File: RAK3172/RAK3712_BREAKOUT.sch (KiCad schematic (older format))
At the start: 3 parts, among them J1 Conn_01x20_Male, J2 Conn_01x20_Male, U1 RAK11300

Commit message: started RAK3172 symbol
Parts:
- removed U1: RAK11300, RAKWIRELESS:RAK11300, symbol RAKWIRELESS:RAK11300
- added U?: RAK3712, RAKWIRELESS:RAK3712, symbol RAKWIRELESS:RAK3712
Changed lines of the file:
@@
 $EndDescr
-$Comp
-L RAKWIRELESS:RAK11300 U1
-U 1 1 61FAC138
-P 5700 3250
-F 0 "U1" H 5700 2061 50  0000 C CNN
-F 1 "RAK11300" H 5700 1970 50  0000 C CNN
-F 2 "RAKWIRELESS:RAK11300" H 5900 3550 50  0001 C CNN
-F 3 "https://site-file.fomillesite.com/1260815565112336386/1427562149389201410.pdf" H 5900 3550 50  0001 C CNN
-	1    5700 3250
-	1    0    0    -1
-$EndComp
 $Comp
 L Connector:Conn_01x20_Male J1
@@
 Wire Wire Line
 	5900 2150 5900 1950
+$Comp
+L RAKWIRELESS:RAK3712 U?
+U 1 1 621E74F6
+P 4100 5900
+F 0 "U?" H 4100 4711 50  0000 C CNN
+F 1 "RAK3712" H 4100 4620 50  0000 C CNN
+F 2 "RAKWIRELESS:RAK3712" H 4300 6200 50  0001 C CNN
+F 3 "https://site-file.fomillesite.com/1260815565112336386/1427562149389201410.pdf" H 4300 6200 50  0001 C CNN
+	1    4100 5900
+	1    0    0    -1
+$EndComp
 $EndSCHEMATC

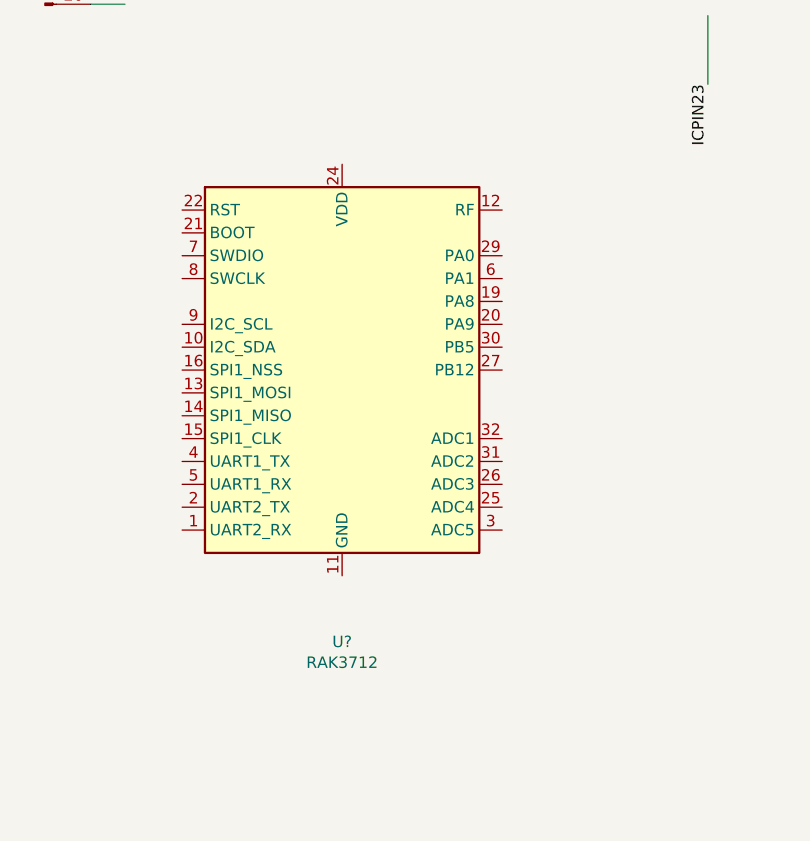
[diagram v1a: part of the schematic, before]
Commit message: sch:(DIL_BREAKOUT_PCB RAK 3712)changing pins
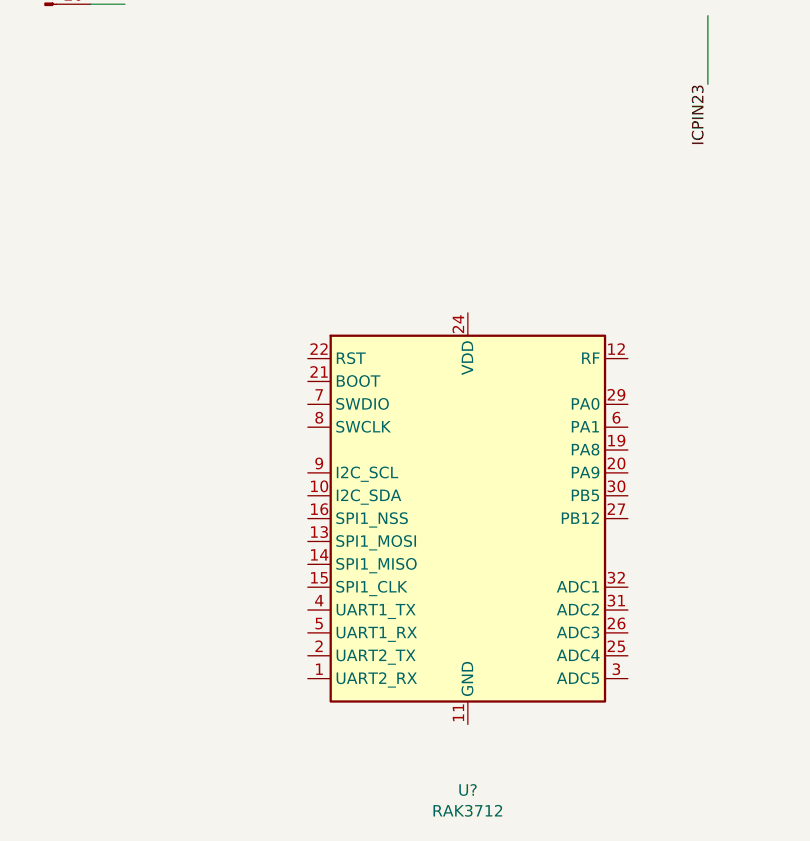
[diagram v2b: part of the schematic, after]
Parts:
- removed U?: RAK3712, RAKWIRELESS:RAK3712, symbol RAKWIRELESS:RAK3712
- added U?: RAK3712, RAKWIRELESS:RAK3712, symbol RAKWIRELESS:RAK3712
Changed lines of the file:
@@
 $Comp
 L RAKWIRELESS:RAK3712 U?
-U 1 1 621E74F6
-P 4100 5900
-F 0 "U?" H 4100 4711 50  0000 C CNN
-F 1 "RAK3712" H 4100 4620 50  0000 C CNN
-F 2 "RAKWIRELESS:RAK3712" H 4300 6200 50  0001 C CNN
-F 3 "https://site-file.fomillesite.com/1260815565112336386/1427562149389201410.pdf" H 4300 6200 50  0001 C CNN
-	1    4100 5900
+U 1 1 621FE862
+P 4650 6550
+F 0 "U?" H 4650 5361 50  0000 C CNN
+F 1 "RAK3712" H 4650 5270 50  0000 C CNN
+F 2 "RAKWIRELESS:RAK3712" H 4850 6850 50  0001 C CNN
+F 3 "https://site-file.fomillesite.com/1260815565112336386/1427562149389201410.pdf" H 4850 6850 50  0001 C CNN
+	1    4650 6550
 	1    0    0    -1
 $EndComp

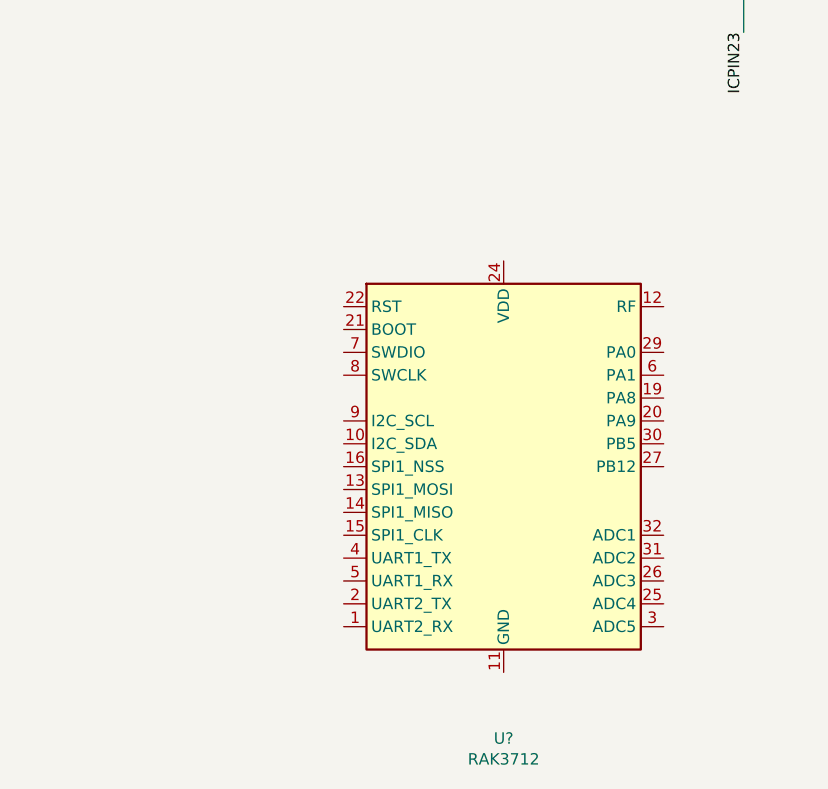
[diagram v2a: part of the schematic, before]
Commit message: sch:(DIL_BREAKOUT_PCB RAK 3712)pins arranged
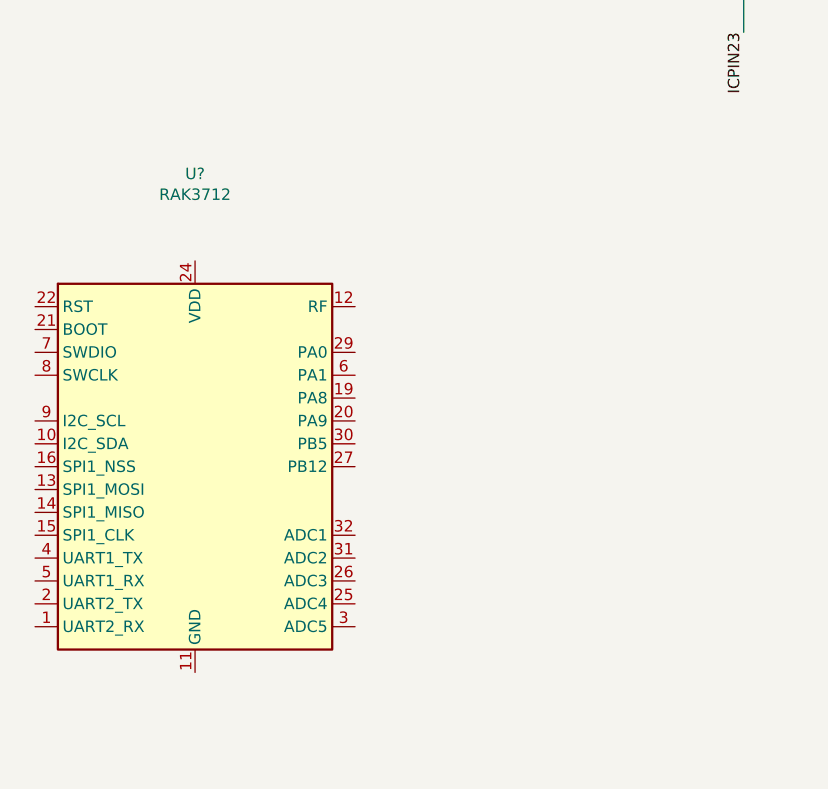
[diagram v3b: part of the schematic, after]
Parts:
- removed U?: RAK3712, RAKWIRELESS:RAK3712, symbol RAKWIRELESS:RAK3712
- added U?: RAK3712, RAKWIRELESS:RAK3712, symbol RAKWIRELESS:RAK3712
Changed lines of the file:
@@
 $Comp
 L RAKWIRELESS:RAK3712 U?
-U 1 1 621FE862
-P 4650 6550
-F 0 "U?" H 4650 5361 50  0000 C CNN
-F 1 "RAK3712" H 4650 5270 50  0000 C CNN
-F 2 "RAKWIRELESS:RAK3712" H 4850 6850 50  0001 C CNN
-F 3 "https://site-file.fomillesite.com/1260815565112336386/1427562149389201410.pdf" H 4850 6850 50  0001 C CNN
-	1    4650 6550
+U 1 1 621F85E6
+P 3300 6550
+F 0 "U?" H 3300 7831 50  0000 C CNN
+F 1 "RAK3712" H 3300 7740 50  0000 C CNN
+F 2 "RAKWIRELESS:RAK3712" H 3500 6850 50  0001 C CNN
+F 3 "https://site-file.fomillesite.com/1260815565112336386/1427562149389201410.pdf" H 3500 6850 50  0001 C CNN
+	1    3300 6550
 	1    0    0    -1
 $EndComp

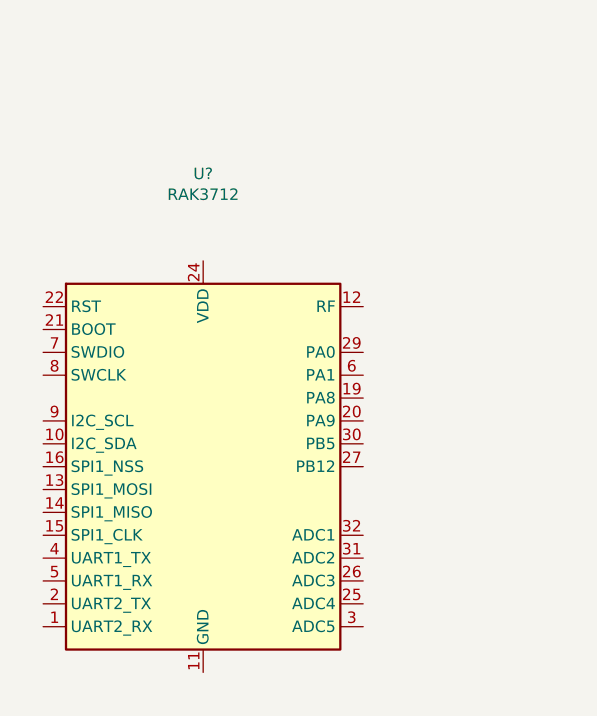
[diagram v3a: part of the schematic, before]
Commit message: sch:(DIL_BREAKOUT_PCB RAK 3712)shrinked
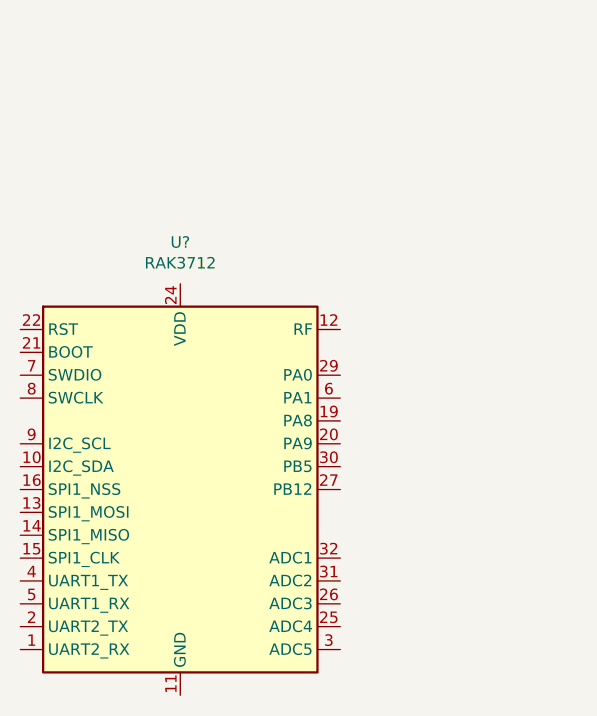
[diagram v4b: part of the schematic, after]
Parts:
- removed U?: RAK3712, RAKWIRELESS:RAK3712, symbol RAKWIRELESS:RAK3712
- added U?: RAK3712, RAKWIRELESS:RAK3712, symbol RAKWIRELESS:RAK3712
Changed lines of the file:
@@
 $Comp
 L RAKWIRELESS:RAK3712 U?
-U 1 1 621F85E6
-P 3300 6550
-F 0 "U?" H 3300 7831 50  0000 C CNN
-F 1 "RAK3712" H 3300 7740 50  0000 C CNN
-F 2 "RAKWIRELESS:RAK3712" H 3500 6850 50  0001 C CNN
-F 3 "https://site-file.fomillesite.com/1260815565112336386/1427562149389201410.pdf" H 3500 6850 50  0001 C CNN
-	1    3300 6550
+U 1 1 621FE0F5
+P 3200 6650
+F 0 "U?" H 3200 7731 50  0000 C CNN
+F 1 "RAK3712" H 3200 7640 50  0000 C CNN
+F 2 "RAKWIRELESS:RAK3712" H 3400 6950 50  0001 C CNN
+F 3 "https://site-file.fomillesite.com/1260815565112336386/1427562149389201410.pdf" H 3400 6950 50  0001 C CNN
+	1    3200 6650
 	1    0    0    -1
 $EndComp

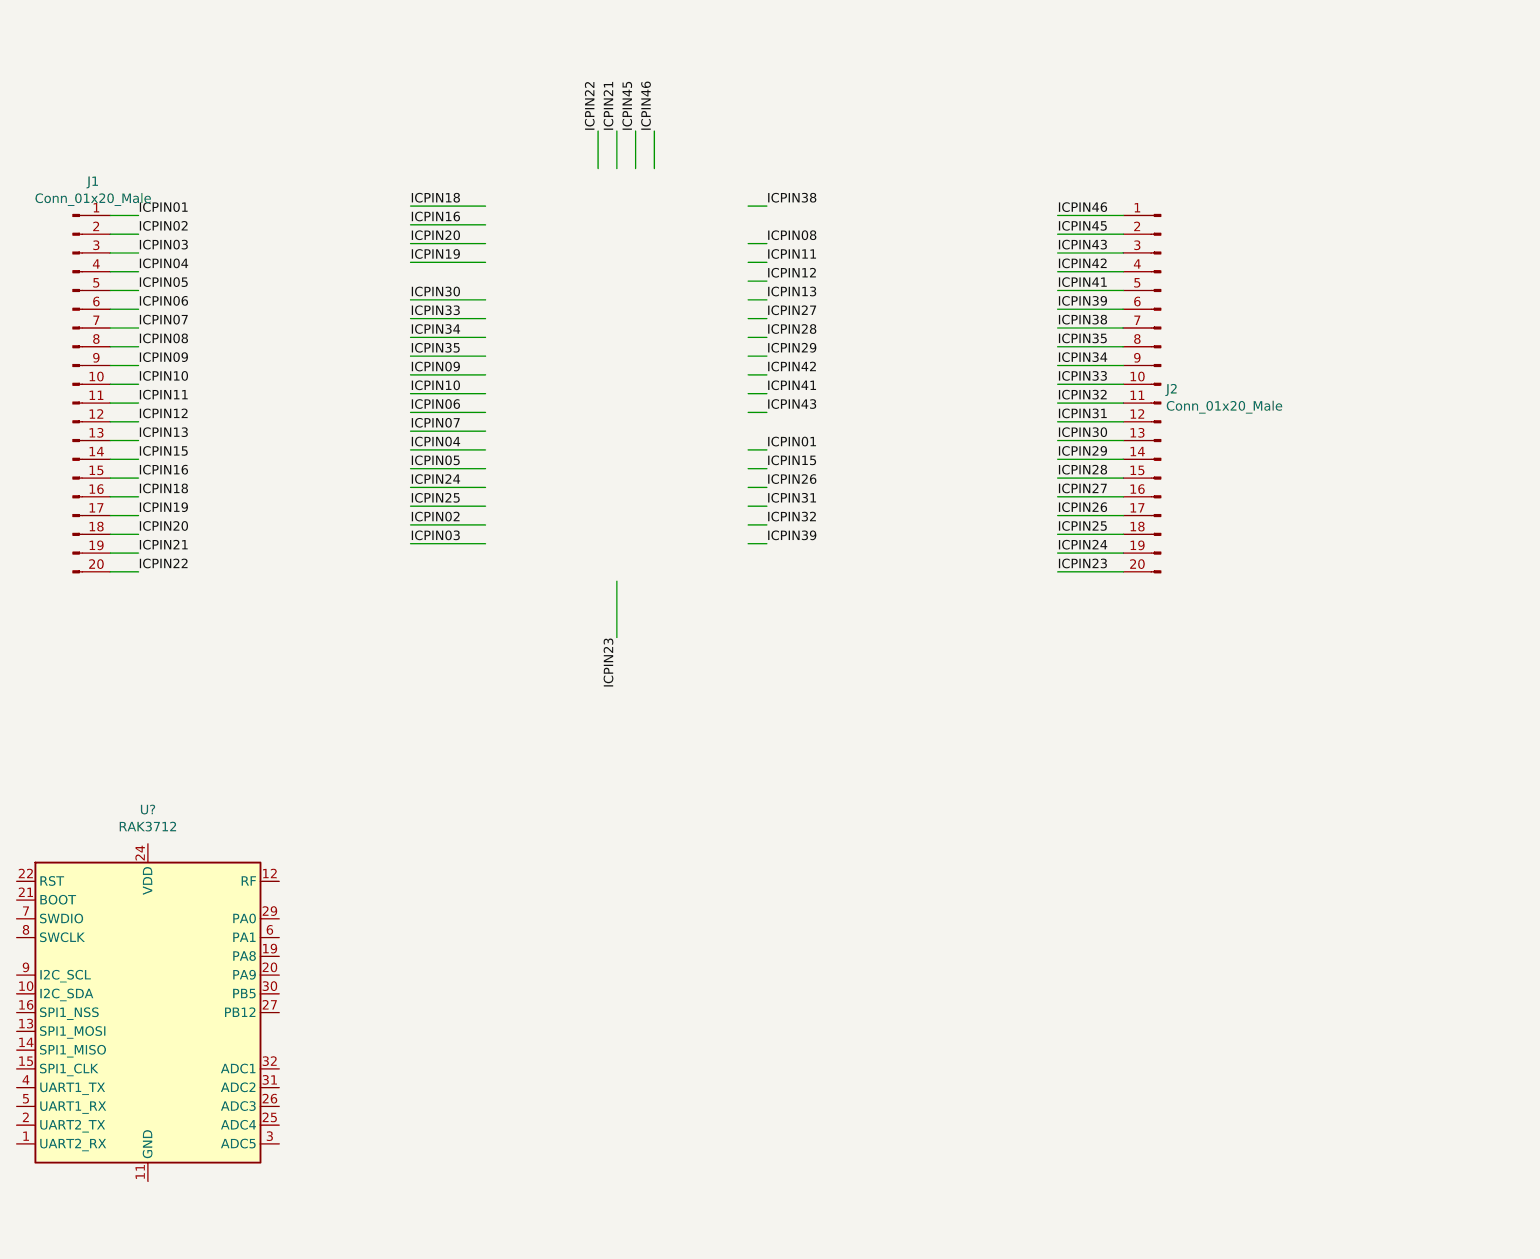
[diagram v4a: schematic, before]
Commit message: sch:(DIL_BREAKOUT_PCB RAK 3712)tied to headers
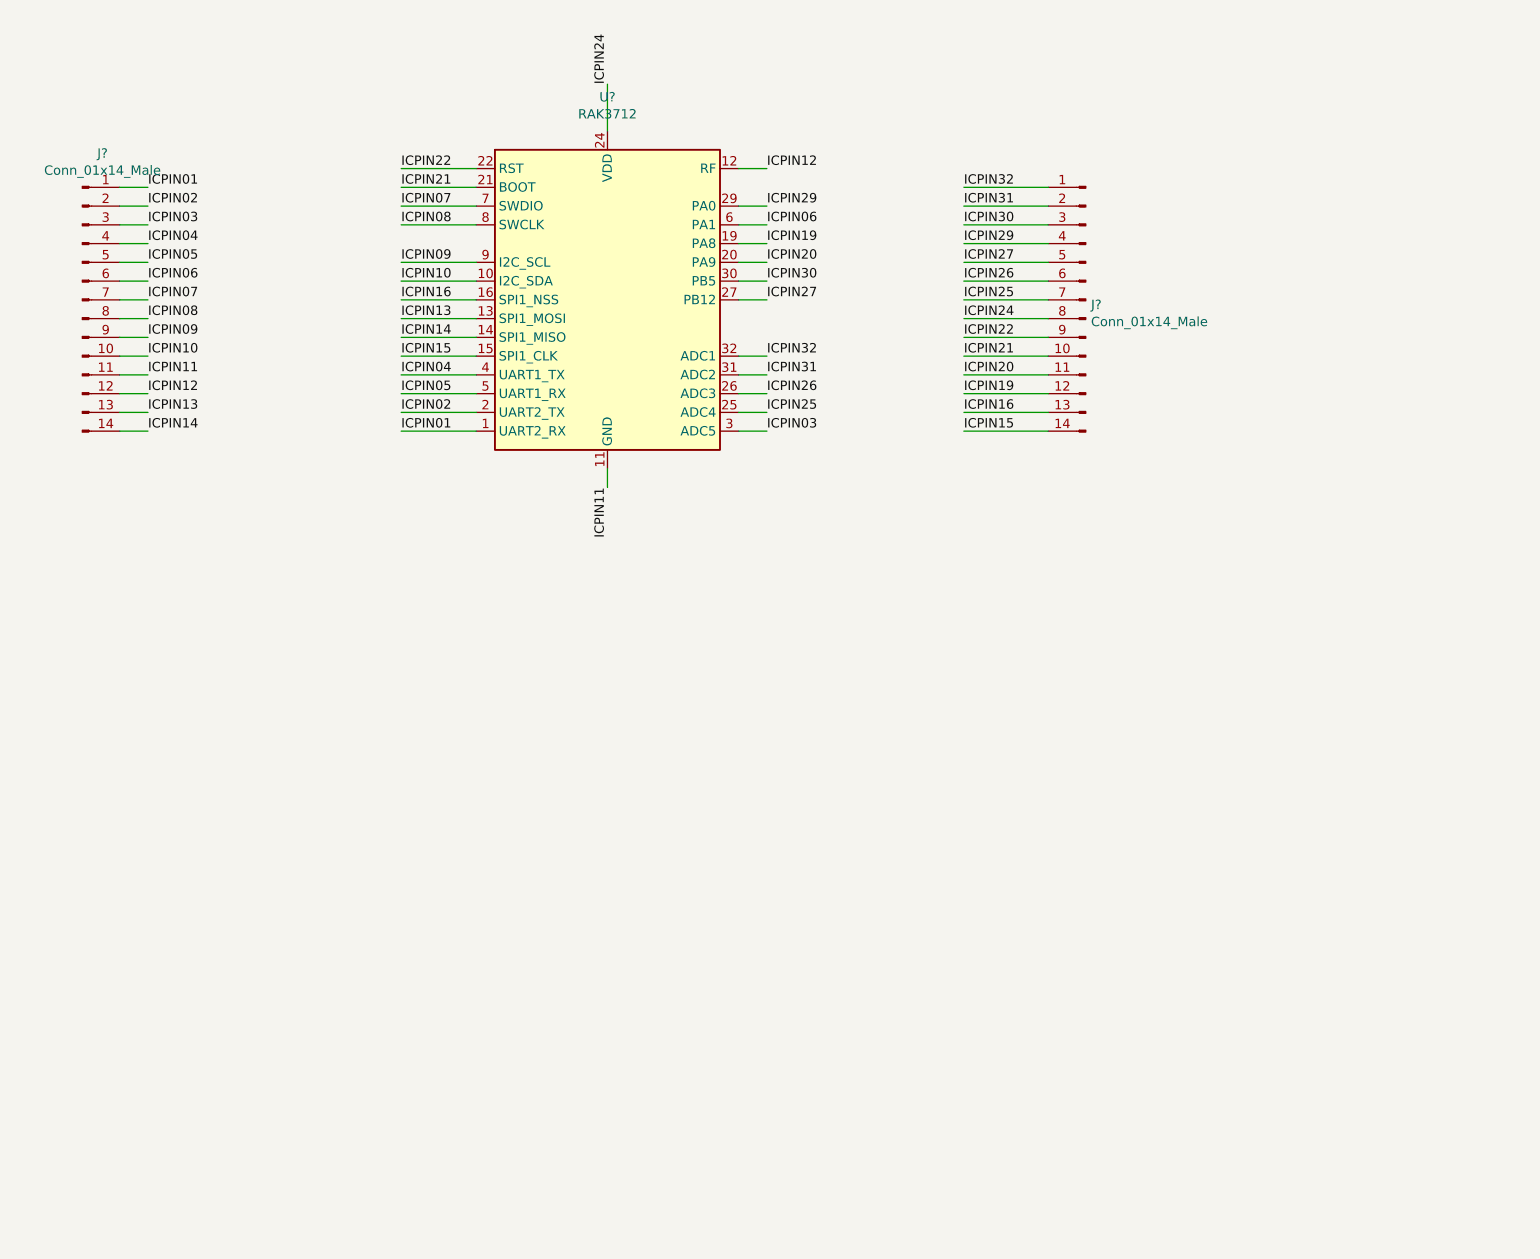
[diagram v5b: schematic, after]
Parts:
- removed J1, J2: Conn_01x20_Male, Connector_PinHeader_2.54mm:PinHeader_1x20_P2.54mm_Vertical, symbol Connector:Conn_01x20_Male
- added J? (x2): Conn_01x14_Male, symbol Connector:Conn_01x14_Male
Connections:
- net labels added: ICPIN14
- net labels removed: ICPIN18, ICPIN23, ICPIN28, ICPIN33, ICPIN34, ICPIN35, ICPIN38, ICPIN39, ICPIN41, ICPIN42, ICPIN43, ICPIN45, ICPIN46
- wire segments 80 -> 56
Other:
- moved on the sheet: U?
